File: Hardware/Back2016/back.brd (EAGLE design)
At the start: 100 x 100 mm, 85 parts, among them J1 RASPBERRYPI-40-PIN-GPIO-SMT, U3 SN74LVC2G34DCKR, U4 2.5V, U5 3.3V

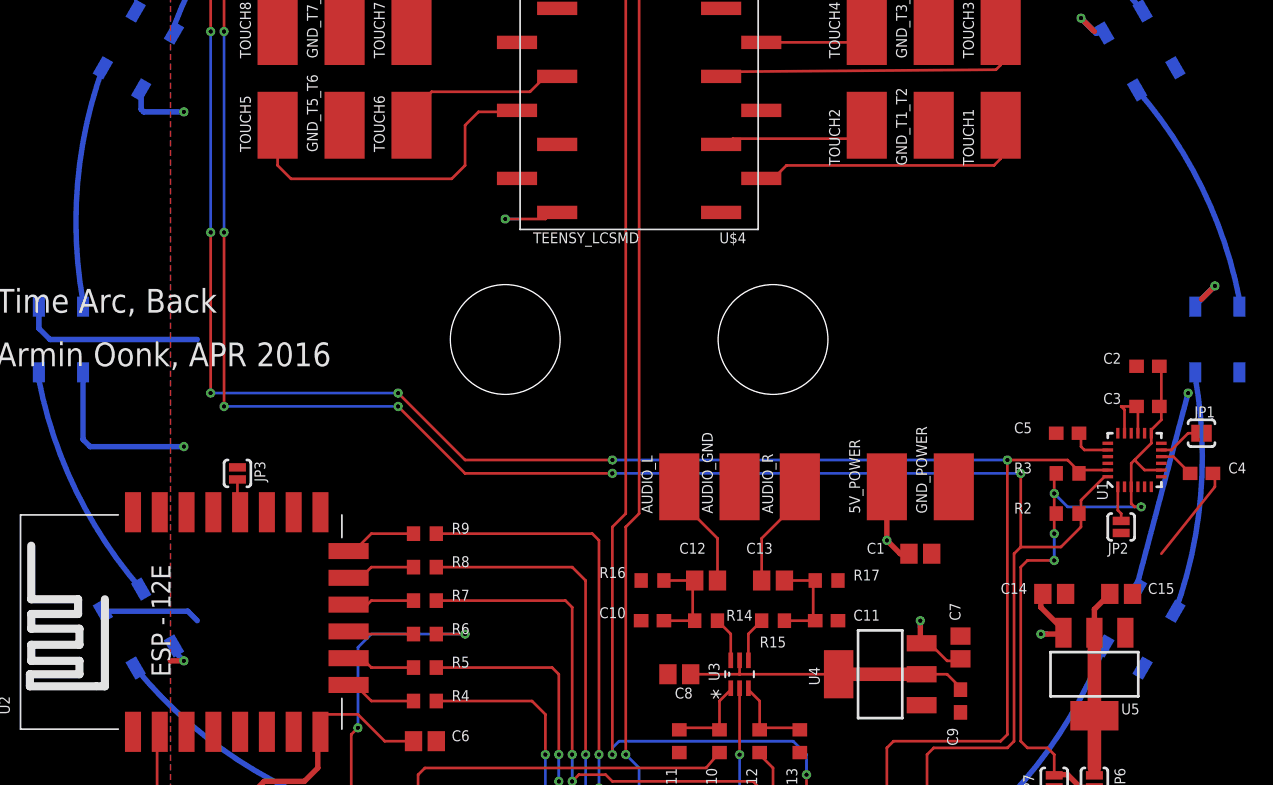
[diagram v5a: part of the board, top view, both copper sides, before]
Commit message: More small tweaks to the silkscreen
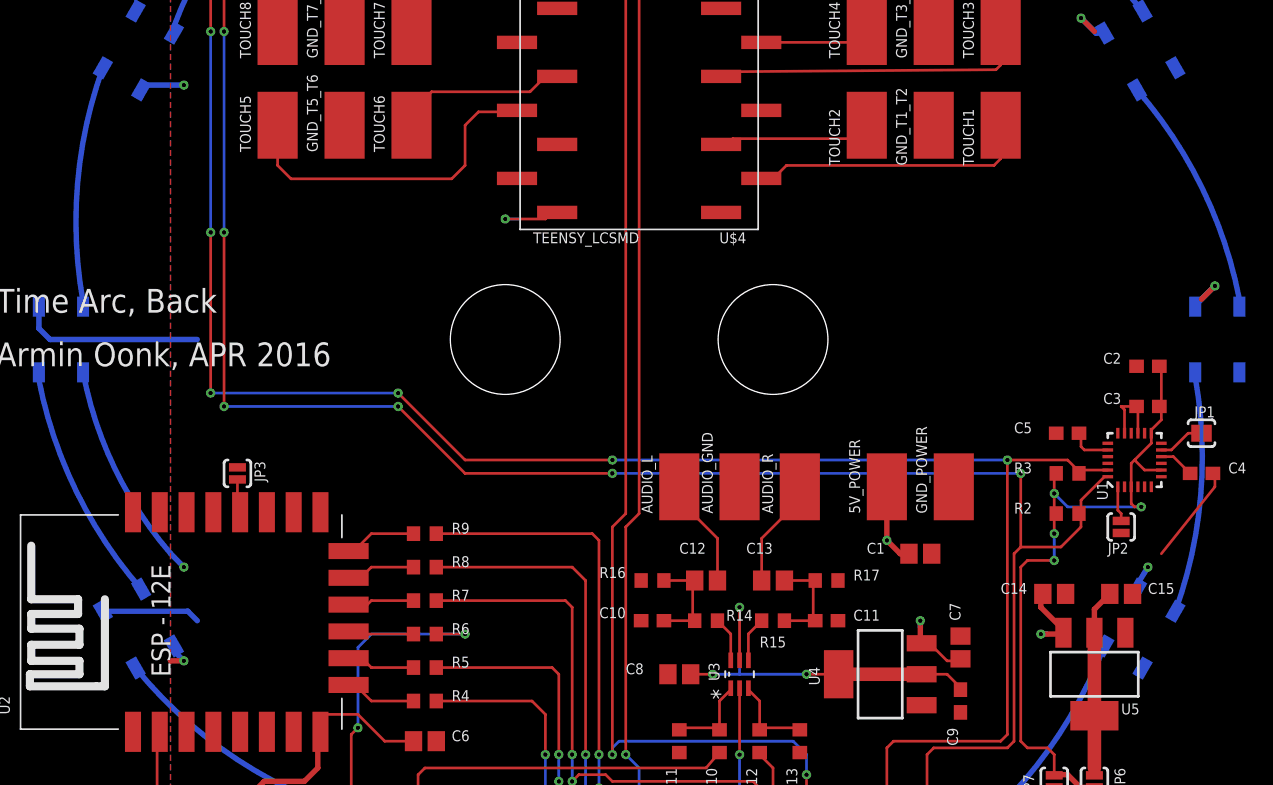
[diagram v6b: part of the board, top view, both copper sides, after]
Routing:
- net GND: track 82.2 -> 72.1 mm
- net 2.5V: track 21.8 -> 29.7 mm, vias 0 -> 3
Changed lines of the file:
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@@
 <layer number="27" name="tValues" color="7" fill="1" visible="yes" active="yes"/>
 <layer number="28" name="bValues" color="7" fill="1" visible="yes" active="yes"/>
-<layer number="29" name="tStop" color="7" fill="3" visible="yes" active="yes"/>
-<layer number="30" name="bStop" color="7" fill="6" visible="yes" active="yes"/>
+<layer number="29" name="tStop" color="7" fill="3" visible="no" active="yes"/>
+<layer number="30" name="bStop" color="7" fill="6" visible="no" active="yes"/>
 <layer number="31" name="tCream" color="7" fill="4" visible="no" active="yes"/>
 <layer number="32" name="bCream" color="7" fill="5" visible="no" active="yes"/>
@@
 <element name="U4" library="SparkFun-PowerIC" package="SOT223" value="2.5V" x="68" y="25" smashed="yes" rot="R90">
 <attribute name="PROD_ID" value="VREG-08170" x="68" y="25" size="1.778" layer="27" rot="R90" display="off"/>
-<attribute name="NAME" x="63.4915" y="24.1745" size="0.8128" layer="25" rot="R90"/>
-<attribute name="VALUE" x="68.1905" y="23.9205" size="0.8128" layer="27" rot="R90"/>
+<attribute name="NAME" x="63.4915" y="24.1745" size="0.8128" layer="25" font="vector" rot="R90"/>
+<attribute name="VALUE" x="68.1905" y="23.9205" size="0.8128" layer="27" font="vector" rot="R90"/>
 </element>
 <element name="C7" library="timearc" package="C0805" value="10u" x="74" y="27" smashed="yes" rot="R90">
@@
 </element>
 <element name="C8" library="timearc" package="C0805" value="10u" x="53" y="25" smashed="yes" rot="R180">
-<attribute name="NAME" x="54" y="24" size="0.8128" layer="25" font="vector" ratio="13" rot="R180"/>
-<attribute name="VALUE" x="54" y="27" size="0.8128" layer="27" font="vector" ratio="13" rot="R180"/>
+<attribute name="NAME" x="49" y="25" size="0.8128" layer="25" font="vector" ratio="13"/>
+<attribute name="VALUE" x="49" y="24" size="0.8128" layer="27" font="vector" ratio="13"/>
 </element>
 <element name="R10" library="timearc" package="R0603" value="100" x="56" y="20" smashed="yes" rot="R90">
@@
 <element name="LED10" library="timearc" package="WS2812B" value="WS2812B5050" x="12.604928125" y="71.5899" locked="yes" smashed="yes" rot="MR120"/>
 <element name="LED11" library="timearc" package="WS2812B" value="WS2812B5050" x="28.4099" y="87.394871875" locked="yes" smashed="yes" rot="MR150"/>
-<element name="LED12" library="timearc" package="WS2812B" value="WS2812B5050" x="49.9999" y="93.1799" locked="yes" smashed="yes" rot="MR180">
-<attribute name="NAME" x="53.4924" y="91.5924" size="0.8128" layer="26" ratio="10" rot="MR90"/>
-</element>
+<element name="LED12" library="timearc" package="WS2812B" value="WS2812B5050" x="49.9999" y="93.1799" locked="yes" smashed="yes" rot="MR180"/>
 <element name="DO_WS1282" library="timearc" package="SOLDER_PAD" value="SOLDER_PAD" x="72" y="94" smashed="yes" rot="R180">
 <attribute name="NAME" x="74" y="96" size="0.8128" layer="21" font="vector" ratio="13" rot="R270"/>
@@
 <wire x1="86" y1="45" x2="87.15" y2="45" width="0.2032" layer="1"/>
 <wire x1="87.19093125" y1="31.356659375" x2="87.19093125" y2="31.69093125" width="0.4064" layer="16"/>
-<wire x1="87.19093125" y1="31.69093125" x2="91" y2="46" width="0.4064" layer="16"/>
-<via x="91" y="46" extent="1-16" drill="0.31"/>
+<wire x1="87.19093125" y1="31.69093125" x2="88" y2="33" width="0.4064" layer="16"/>
+<via x="88" y="33" extent="1-16" drill="0.31"/>
 <wire x1="91.5299" y1="52.4499" x2="91.5299" y2="52.5299" width="0.4064" layer="16"/>
 <wire x1="91.5299" y1="52.5299" x2="93" y2="54" width="0.4064" layer="16"/>
@@
 <via x="26" y="83" extent="1-16" drill="0.31"/>
 <wire x1="26" y1="83" x2="27" y2="84" width="0.4064" layer="1"/>
-<wire x1="12.808871875" y1="68.6431375" x2="12.808871875" y2="67.191128125" width="0.4064" layer="16"/>
-<wire x1="12.808871875" y1="67.191128125" x2="13" y2="67" width="0.4064" layer="16"/>
-<wire x1="13" y1="67" x2="16" y2="67" width="0.4064" layer="16"/>
-<via x="16" y="67" extent="1-16" drill="0.31"/>
+<wire x1="12.808871875" y1="68.6431375" x2="12.808871875" y2="68.191128125" width="0.4064" layer="16"/>
+<wire x1="12.808871875" y1="68.191128125" x2="13" y2="69" width="0.4064" layer="16"/>
+<wire x1="13" y1="69" x2="16" y2="69" width="0.4064" layer="16"/>
+<via x="16" y="69" extent="1-16" drill="0.31"/>
 <wire x1="31.3566625" y1="12.80886875" x2="31.3566625" y2="10.6433375" width="0.4064" layer="16"/>
 <wire x1="31.3566625" y1="10.6433375" x2="32" y2="10" width="0.4064" layer="16"/>
@@
 <via x="16" y="26" extent="1-16" drill="0.31"/>
 <wire x1="16" y1="26" x2="15" y2="26" width="0.4064" layer="1"/>
-<wire x1="8.4699" y1="47.5499" x2="8.4699" y2="42.5301" width="0.4064" layer="16"/>
-<wire x1="8.4699" y1="42.5301" x2="9" y2="42" width="0.4064" layer="16"/>
-<wire x1="9" y1="42" x2="16" y2="42" width="0.4064" layer="16"/>
-<via x="16" y="42" extent="1-16" drill="0.31"/>
+<via x="16" y="33" extent="1-16" drill="0.31"/>
 <contactref element="U5" pad="1"/>
 <contactref element="C14" pad="2"/>
@@
 <via x="57.5" y="16" extent="1-16" drill="0.31"/>
 <wire x1="57.5" y1="16" x2="57.5" y2="15.5" width="0.2032" layer="1"/>
+<wire x1="8.4699" y1="47.5499" x2="15.0198" y2="34" width="0.4064" layer="16" curve="30"/>
+<wire x1="15.0198" y1="34" x2="16" y2="33" width="0.4064" layer="16"/>
 </signal>
 <signal name="5V">
@@
 <contactref element="U3" pad="5"/>
 <contactref element="C9" pad="1"/>
-<wire x1="53.85" y1="25" x2="57.5" y2="25" width="0.2032" layer="1"/>
-<wire x1="57.5" y1="25" x2="64.901" y2="25" width="0.2032" layer="1"/>
-<wire x1="57.5" y1="26.0414" x2="57.5" y2="25" width="0.2032" layer="1"/>
 <wire x1="71.0988" y1="25" x2="64.901" y2="25" width="1.016" layer="1"/>
 <wire x1="71.0988" y1="25" x2="73" y2="25" width="0.2032" layer="1"/>
 <wire x1="73" y1="25" x2="74" y2="24" width="0.2032" layer="1"/>
 <wire x1="74" y1="24" x2="74" y2="23.85" width="0.2032" layer="1"/>
+<wire x1="64.901" y1="25" x2="62.5" y2="25" width="0.2032" layer="1"/>
+<via x="62.5" y="25" extent="1-16" drill="0.31"/>
+<wire x1="62.5" y1="25" x2="57.5" y2="25" width="0.2032" layer="16"/>
+<via x="55.5" y="25" extent="1-16" drill="0.31"/>
+<wire x1="57.5" y1="25" x2="55.5" y2="25" width="0.2032" layer="16"/>
+<wire x1="55.5" y1="25" x2="53.85" y2="25" width="0.2032" layer="1"/>
+<wire x1="57.5" y1="26.0414" x2="57.5" y2="30" width="0.2032" layer="1"/>
+<via x="57.5" y="30" extent="1-16" drill="0.31"/>
+<wire x1="57.5" y1="30" x2="57.5" y2="25" width="0.2032" layer="16"/>
 </signal>
 <signal name="N$13">

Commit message: Finished hardware design, added logo
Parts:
- added U$1: (no value), timearc:TIMEARC_LOGO
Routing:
- net 5V: track 67.9 -> 67.4 mm
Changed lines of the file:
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@@
 <element name="U4" library="SparkFun-PowerIC" package="SOT223" value="2.5V" x="68" y="25" smashed="yes" rot="R90">
 <attribute name="PROD_ID" value="VREG-08170" x="68" y="25" size="1.778" layer="27" rot="R90" display="off"/>
-<attribute name="NAME" x="63.4915" y="24.1745" size="0.8128" layer="25" font="vector" rot="R90"/>
-<attribute name="VALUE" x="68.1905" y="23.9205" size="0.8128" layer="27" font="vector" rot="R90"/>
+<attribute name="NAME" x="64" y="23" size="0.8128" layer="25" font="vector" rot="R270"/>
+<attribute name="VALUE" x="65" y="23" size="0.8128" layer="27" font="vector" rot="R270"/>
 </element>
 <element name="C7" library="timearc" package="C0805" value="10u" x="74" y="27" smashed="yes" rot="R90">
@@
 <attribute name="NAME" x="79.5" y="16" size="0.8128" layer="25" font="vector" ratio="13" rot="R90"/>
 </element>
+<element name="U$1" library="timearc" package="TIMEARC_LOGO" value="" x="100" y="0" rot="MR0"/>
 </elements>
 <signals>
@@
 <wire x1="5.1699" y1="50.8301" x2="6" y2="50" width="0.4064" layer="16"/>
 <wire x1="6" y1="50" x2="17" y2="50" width="0.4064" layer="16"/>
-<wire x1="12.4009875" y1="74.536659375" x2="12.4009875" y2="75.4009875" width="0.2032" layer="16"/>
-<wire x1="12.4009875" y1="75.4009875" x2="16" y2="79" width="0.2032" layer="16" curve="-30"/>
+<wire x1="12.4009875" y1="74.536659375" x2="12.4009875" y2="74.9009875" width="0.2032" layer="16"/>
+<wire x1="12.4009875" y1="74.9009875" x2="16" y2="78.5" width="0.4064" layer="16" curve="-30"/>
 <wire x1="67" y1="94" x2="64" y2="94" width="0.4064" layer="1"/>
 <via x="64" y="94" extent="1-16" drill="0.31"/>

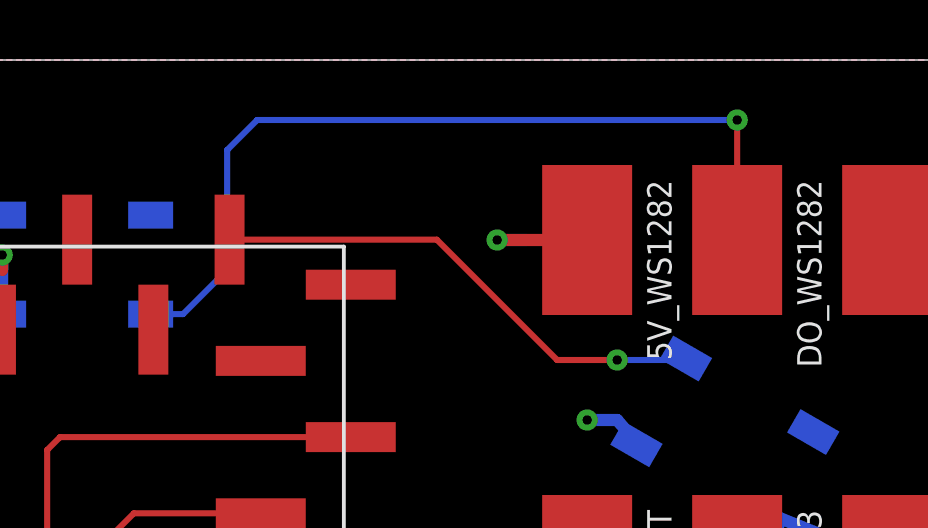
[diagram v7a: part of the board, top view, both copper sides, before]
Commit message: Increase logo resolution
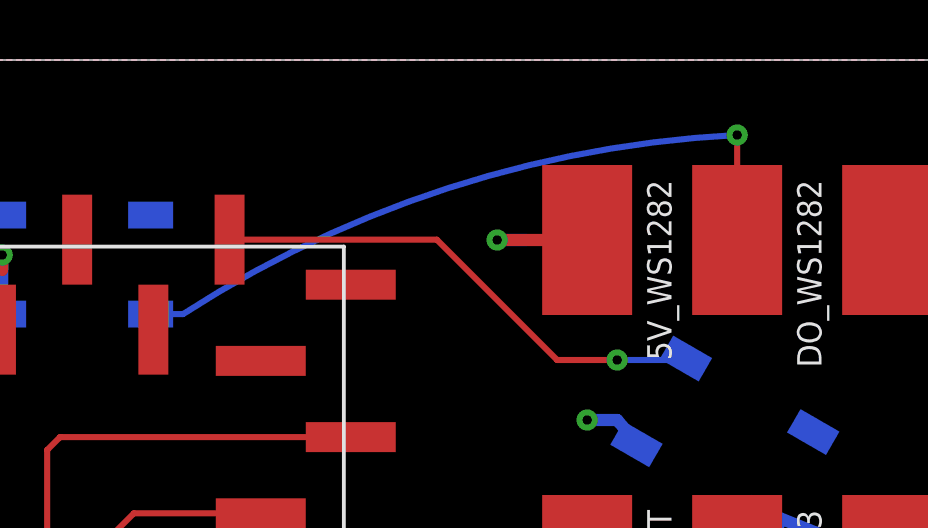
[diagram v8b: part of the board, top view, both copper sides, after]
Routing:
- net N$43: track 28.6 -> 24.0 mm
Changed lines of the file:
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@@
 <contactref element="U$4" pad="P17_5V"/>
 <contactref element="LED1" pad="4-DIN"/>
-<wire x1="55.08" y1="94.0114" x2="61.9886" y2="94.0114" width="0.2032" layer="1"/>
 <wire x1="61.9886" y1="94.0114" x2="66" y2="90" width="0.2032" layer="1"/>
 <wire x1="66" y1="90" x2="68" y2="90" width="0.2032" layer="1"/>
@@
 <wire x1="68" y1="90" x2="70.244328125" y2="90" width="0.2032" layer="16"/>
 <wire x1="70.244328125" y1="90" x2="70.293140625" y2="90.0488125" width="0.2032" layer="16"/>
+<wire x1="55.08" y1="94.0114" x2="61.9886" y2="94.0114" width="0.2032" layer="1"/>
 </signal>
 <signal name="N$18">
@@
 <contactref element="DO_WS1282" pad="1"/>
 <wire x1="52.4499" y1="91.5299" x2="53.5299" y2="91.5299" width="0.2032" layer="16"/>
-<wire x1="53.5299" y1="91.5299" x2="55" y2="93" width="0.2032" layer="16"/>
-<wire x1="55" y1="93" x2="55" y2="97" width="0.2032" layer="16"/>
-<wire x1="55" y1="97" x2="56" y2="98" width="0.2032" layer="16"/>
-<wire x1="56" y1="98" x2="72" y2="98" width="0.2032" layer="16"/>
-<via x="72" y="98" extent="1-16" drill="0.31"/>
-<wire x1="72" y1="98" x2="72" y2="94" width="0.2032" layer="1"/>
+<via x="72" y="97.5" extent="1-16" drill="0.31"/>
+<wire x1="72" y1="97.5" x2="72" y2="94" width="0.2032" layer="1"/>
+<wire x1="53.5299" y1="91.5299" x2="72" y2="97.5" width="0.2032" layer="16" curve="-30"/>
 </signal>
 <signal name="N$44">
